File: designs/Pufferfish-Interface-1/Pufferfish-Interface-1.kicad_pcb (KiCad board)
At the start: 2 copper layers, 0 parts

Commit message: beginning layout
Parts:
- added BUZZ1: BUZZER-MALLORY, Pufferfish:Buzzer-MSS5MMG, F.Cu at (95.2, 69.8)
- added BUZZ2: BUZZER, Pufferfish:Buzzer_PS1927P02, F.Cu at (127.0, 68.6)
- added C1: 0.1uF, Pufferfish:CAP_SMD_0805, F.Cu at (121.5, 150.1)
- added C2: 0.1uF, Pufferfish:CAP_SMD_0805, F.Cu at (117.1, 153.0)
- added CONN1: 5103308-3, Pufferfish:SHDR16W66P254_2X8, F.Cu at (186.8, 98.8)
- added CONN2: B2B-PH-SM4-TB(LF)(SN), Pufferfish:JST_B2B-PH-SM4-TB, F.Cu at (109.8, 151.2)
- added CONN3: B2B-PH-SM4-TB(LF)(SN), Pufferfish:JST_B2B-PH-SM4-TB, F.Cu at (99.8, 151.2)
- added D1: 1N4001, Diode_THT:D_DO-41_SOD81_P10.16mm_Horizontal, F.Cu at (96.6, 121.1)
- added D10: LED_RGBA, Pufferfish:LED_D10.0mm-4_RGB, F.Cu at (149.1, 100.7)
- added D2: 1N4001, Diode_THT:D_DO-41_SOD81_P10.16mm_Horizontal, F.Cu at (110.5, 121.1)
- added D3: LED, Pufferfish:LED_SMD_1411_3528, F.Cu at (126.4, 121.2)
- added D4: LED, Pufferfish:LED_SMD_1411_3528, F.Cu at (106.2, 125.4)
- added D5: LED, Pufferfish:LED_SMD_1411_3528, F.Cu at (98.6, 125.4)
- added D6: TPD1E1B04, Pufferfish:D_0402_TPD1E1B04DPYR, F.Cu at (120.7, 152.5)
- added D7: TPD1E1B04, Pufferfish:D_0402_TPD1E1B04DPYR, F.Cu at (125.1, 148.6)
- added D8: TPD1E1B04, Pufferfish:D_0402_TPD1E1B04DPYR, F.Cu at (128.2, 144.4)
- added D9: TPD1E1B04, Pufferfish:D_0402_TPD1E1B04DPYR, F.Cu at (125.1, 146.6)
- added Q1: DMN10H220L, Package_TO_SOT_SMD:SOT-23, F.Cu at (118.7, 125.5)
- added Q10: 2N7002E, Package_TO_SOT_SMD:SOT-23, F.Cu at (132.1, 125.8)
- added Q2: DMN10H220L, Package_TO_SOT_SMD:SOT-23, F.Cu at (145.4, 108.9)
- added Q3: DMN10H220L, Package_TO_SOT_SMD:SOT-23, F.Cu at (132.4, 121.2)
- added Q4: 2SC1815, Package_TO_SOT_THT:TO-92_Inline, F.Cu at (112.0, 126.5)
- added Q5: 2N7002E, Package_TO_SOT_SMD:SOT-23, F.Cu at (123.2, 125.6)
- added Q6: 2N7002E, Package_TO_SOT_SMD:SOT-23, F.Cu at (157.3, 97.0)
- added Q7: 2N7002E, Package_TO_SOT_SMD:SOT-23, F.Cu at (127.6, 125.6)
- added Q8: 2N7002E, Package_TO_SOT_SMD:SOT-23, F.Cu at (145.4, 113.5)
- added Q9: 2N7002E, Package_TO_SOT_SMD:SOT-23, F.Cu at (136.9, 121.2)
- added R1: RES_SMD_0805, Pufferfish:RES_SMD_0805, F.Cu at (157.3, 103.7)
- added R10: RES_SMD_0805, Pufferfish:RES_SMD_0805, F.Cu at (127.5, 129.4)
- added R11: RES_SMD_0805, Pufferfish:RES_SMD_0805, F.Cu at (123.1, 129.4)
- added R12: RES_SMD_0805, Pufferfish:RES_SMD_0805, F.Cu at (118.7, 129.2)
- added R13: RES_SMD_0805, Pufferfish:RES_SMD_0805, F.Cu at (129.0, 136.0)
- added R14: RES_SMD_0805, Pufferfish:RES_SMD_0805, F.Cu at (117.1, 147.1)
- added R15: RES_SMD_0805, Pufferfish:RES_SMD_0805, F.Cu at (129.0, 139.0)
- added R16: RES_SMD_0805, Pufferfish:RES_SMD_0805, F.Cu at (117.1, 150.1)
- added R17: RES_SMD_0805, Pufferfish:RES_SMD_0805, F.Cu at (121.5, 147.1)
- added R18: RES_SMD_0805, Pufferfish:RES_SMD_0805, F.Cu at (129.0, 141.9)
- added R19: RES_SMD_0805, Pufferfish:RES_SMD_0805, F.Cu at (105.8, 129.1)
- added R2: RES_SMD_0805, Pufferfish:RES_SMD_0805, F.Cu at (154.2, 108.1)
- added R20: RES_SMD_0805, Pufferfish:RES_SMD_0805, F.Cu at (157.3, 100.8)
- added R21: RES_SMD_0805, Pufferfish:RES_SMD_0805, F.Cu at (97.0, 129.1)
- added R22: RES_SMD_0805, Pufferfish:RES_SMD_0805, F.Cu at (101.4, 129.1)
- added R23: RES_SMD_0805, Pufferfish:RES_SMD_0805, F.Cu at (149.8, 108.1)
- added R24: RES_SMD_0805, Pufferfish:RES_SMD_0805, F.Cu at (145.4, 117.2)
- added R3: RES_SMD_0805, Pufferfish:RES_SMD_0805, F.Cu at (149.8, 111.1)
- added R4: RES_SMD_0805, Pufferfish:RES_SMD_0805, F.Cu at (136.5, 125.0)
- added R5: RES_SMD_0805, Pufferfish:RES_SMD_0805, F.Cu at (131.9, 129.5)
- added R6: RES_SMD_0805, Pufferfish:RES_SMD_0805, F.Cu at (141.3, 120.4)
- added R7: RES_SMD_0805, Pufferfish:RES_SMD_0805, F.Cu at (141.3, 123.4)
- added R8: RES_SMD_0805, Pufferfish:RES_SMD_0805, F.Cu at (136.5, 127.9)
- added R9: RES_SMD_0805, Pufferfish:RES_SMD_0805, F.Cu at (154.2, 111.1)
- added SW1: SW_Push, Pufferfish:SW_SPST_SMD_5ESH935, F.Cu at (102.8, 140.1)
- added SW2: SW_Push, Pufferfish:SW_SPST_SMD_5ESH935, F.Cu at (118.8, 140.1)

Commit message: placement started
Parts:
- moved R16 171.2 mm to (261.6, 58.4)
- moved SW2 164.9 mm to (266.7, 67.3)
- moved R17 155.8 mm to (268.0, 94.0)
- moved SW1 152.8 mm to (237.4, 67.7)
- moved C2 149.9 mm to (254.3, 92.7)
- moved D9 139.6 mm to (246.4, 77.5), turned to 90 degrees
- moved C1 136.6 mm to (241.0, 83.8)
- moved D7 127.8 mm to (240.0, 92.7)
- moved R13 117.2 mm to (221.0, 63.5)
- moved R15 117.0 mm to (226.1, 73.7)
- moved Q8 106.1 mm to (47.0, 73.7), turned to 90 degrees
- moved R5 92.7 mm to (133.7, 36.8)
- moved D10 92.2 mm to (64.8, 63.5)
- moved Q4 90.4 mm to (193.0, 86.4), turned to 90 degrees
- moved R24 87.2 mm to (69.8, 73.7)
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
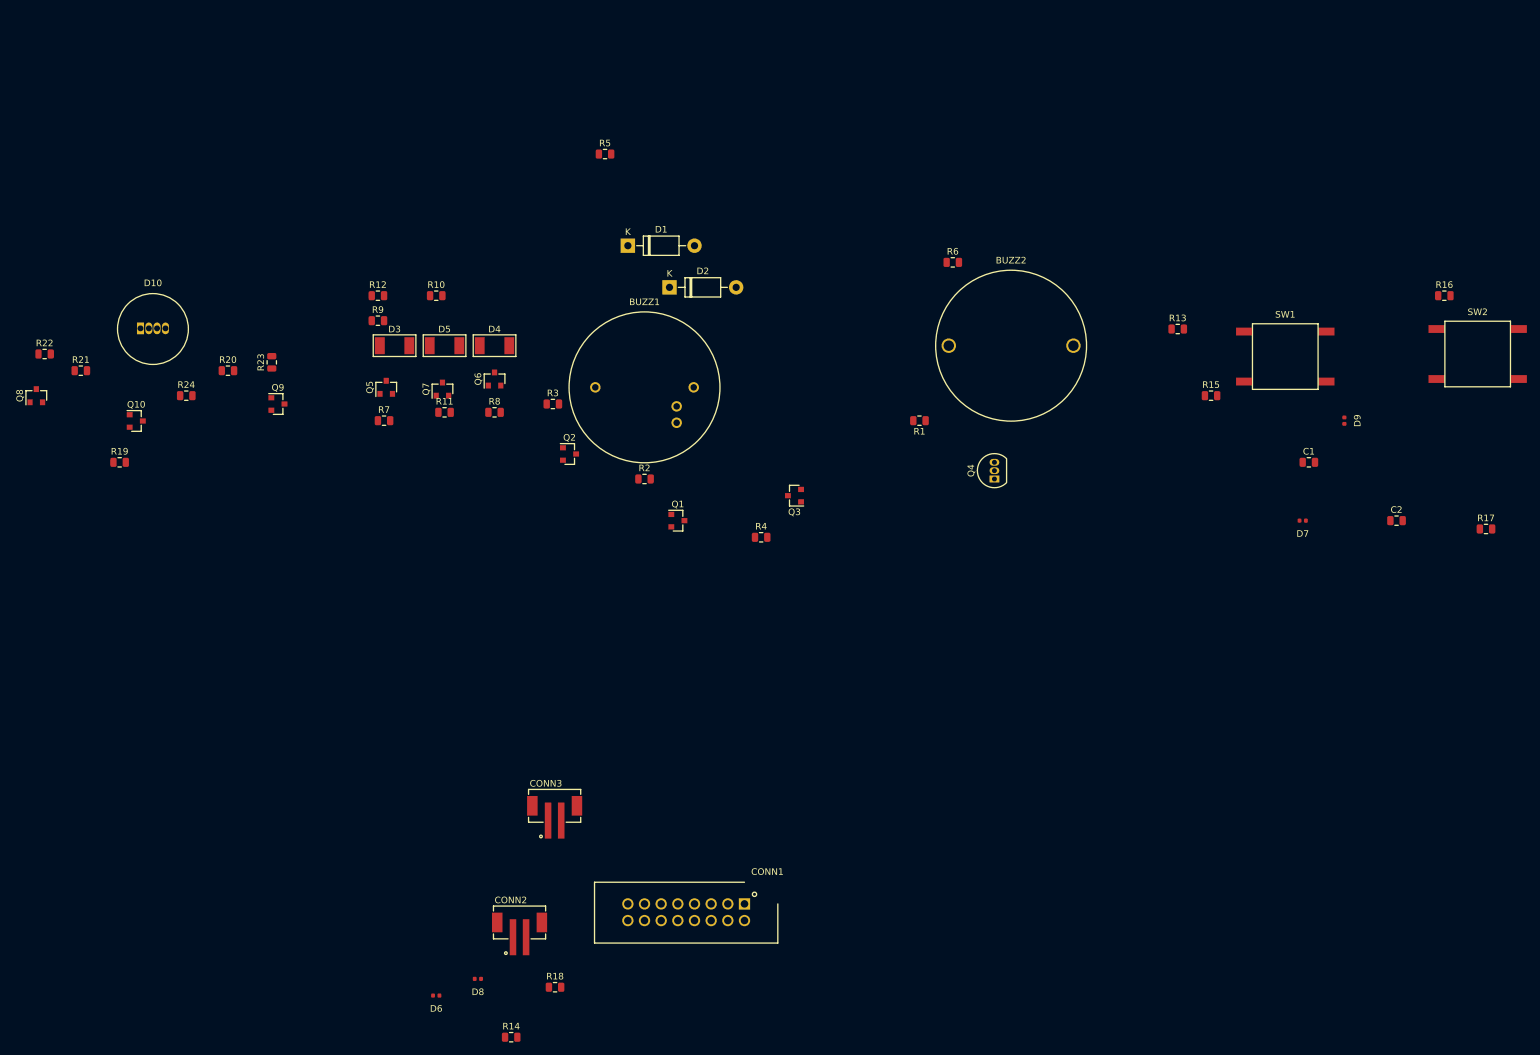
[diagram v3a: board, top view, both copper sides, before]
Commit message: new switches and pcb layout started
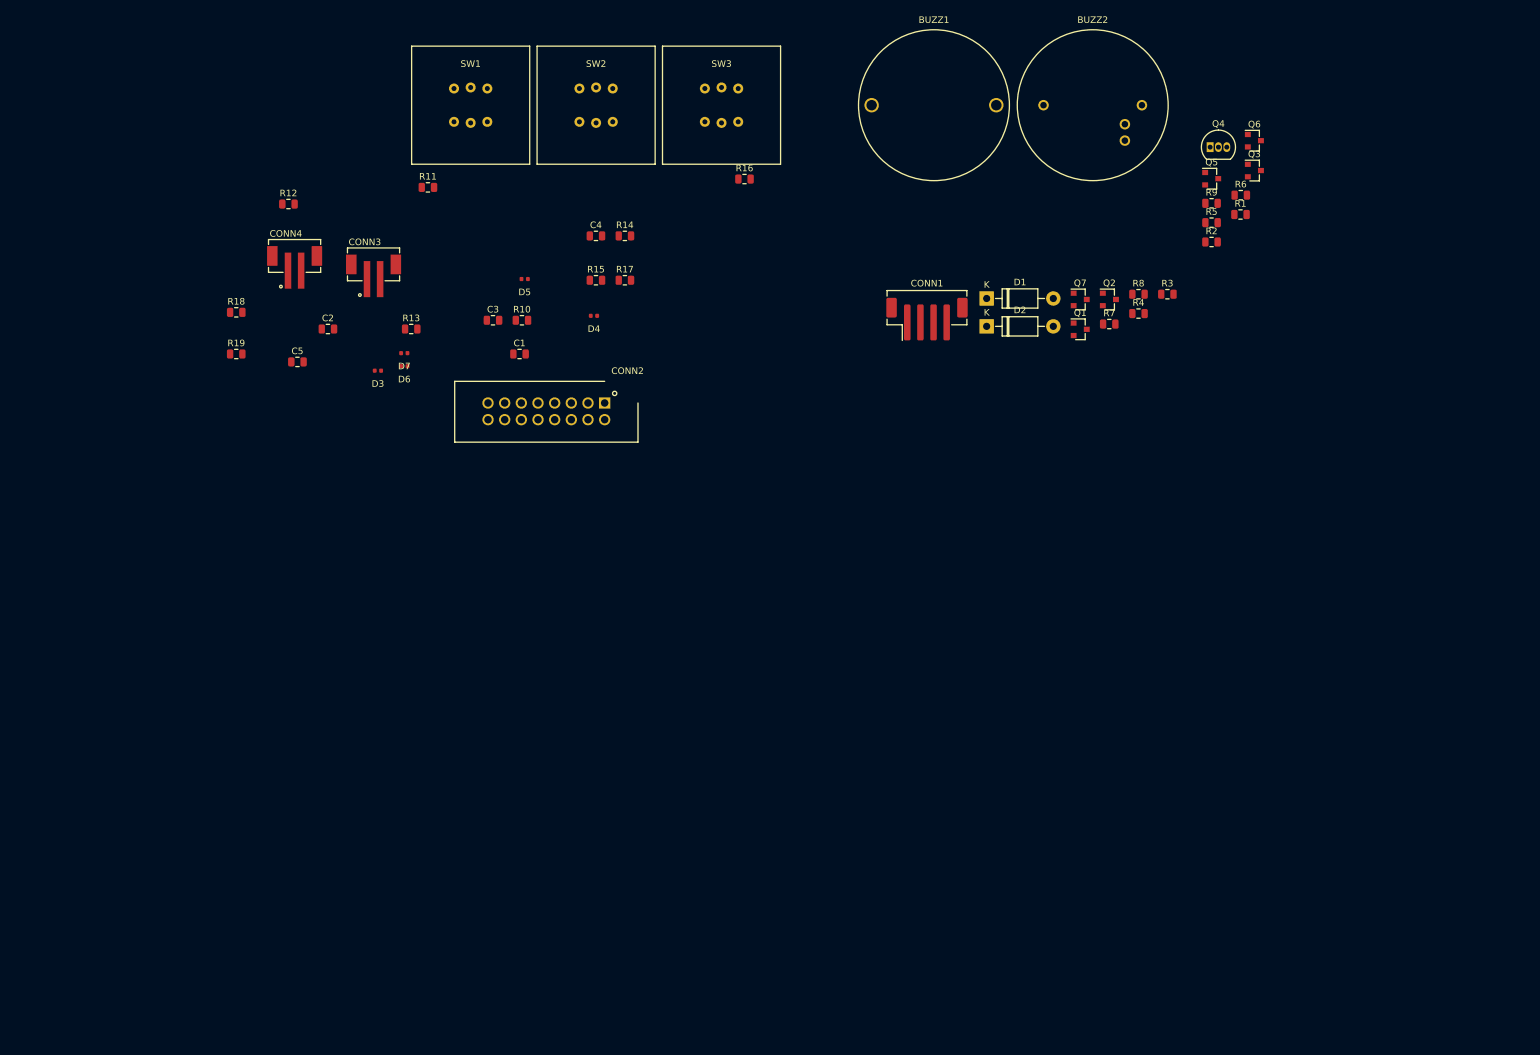
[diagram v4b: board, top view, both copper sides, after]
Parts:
- removed D10: LED_RGBA, Pufferfish:LED_D10.0mm-4_RGB
- removed D8, D9: TPD1E1B04, Pufferfish:D_0402_TPD1E1B04DPYR
- removed Q10, Q8, Q9: 2N7002E, Package_TO_SOT_SMD:SOT-23
- removed R20, R21, R22, R23, R24: RES_SMD_0805, Pufferfish:RES_SMD_0805
- added C3: 0.1uF, Pufferfish:CAP_SMD_0805, F.Cu at (116.6, 62.2)
- added C4: 0.1uF, Pufferfish:CAP_SMD_0805, F.Cu at (132.3, 49.3)
- added C5: 0.1uF, Pufferfish:CAP_SMD_0805, F.Cu at (86.8, 68.5)
- added CONN4: B2B-PH-SM4-TB(LF)(SN), Pufferfish:JST_B2B-PH-SM4-TB, F.Cu at (86.4, 54.6)
- added SW3: SW_Push, Pufferfish:SW_SPST_TC013, F.Cu at (151.4, 29.4)
- BUZZ1: value BUZZER-MALLORY -> BUZZER; footprint Pufferfish:Buzzer-MSS5MMG -> Pufferfish:Buzzer_PS1927P02
- BUZZ2: value BUZZER -> BUZZER-MALLORY; footprint Pufferfish:Buzzer_PS1927P02 -> Pufferfish:Buzzer-MSS5MMG
- CONN1: value 5103308-3 -> B4B-PH-SM4-TB(LF)(SN); footprint Pufferfish:SHDR16W66P254_2X8 -> Connector_JST:JST_PH_B4B-PH-SM4-TB_1x04-1MP_P2.00mm_Vertical
- CONN2: value B2B-PH-SM4-TB(LF)(SN) -> 5103308-3; footprint Pufferfish:JST_B2B-PH-SM4-TB -> Pufferfish:SHDR16W66P254_2X8
- D3, D4, D5: value LED -> TPD1E1B04; footprint Pufferfish:LED_SMD_1411_3528 -> Pufferfish:D_0402_TPD1E1B04DPYR
- SW1, SW2: footprint Pufferfish:SW_SPST_SMD_5ESH935 -> Pufferfish:SW_SPST_TC013
- moved C2 165.5 mm to (91.4, 63.5)
- moved SW2 139.6 mm to (132.3, 29.4)
- moved D7 139.3 mm to (103.1, 67.2)
- moved R17 136.6 mm to (136.7, 56.1)
- moved SW1 129.9 mm to (113.2, 29.4)
- moved Q5 129.8 mm to (226.2, 40.6), turned to 0 degrees
- moved R9 128.3 mm to (226.1, 44.3)
- moved R14 123.4 mm to (136.7, 49.3)
- moved C1 121.4 mm to (120.7, 67.3)
- moved Q6 121.4 mm to (232.7, 34.8), turned to 0 degrees
- moved R13 116.8 mm to (104.1, 63.5)
- moved R18 113.8 mm to (77.5, 61.0)
- moved R7 111.5 mm to (210.5, 62.7)
- moved R16 108.2 mm to (154.9, 40.6)
- moved R8 99.8 mm to (215.0, 58.2)
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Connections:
- BUZZ1 pad 1: 5V -> Net-(BUZZ1-Pad1)
- C2 pad 1: SET_NOT_PAUSE -> SET_PWR_ON_OFF
- CONN1 pad 2: 5V -> Net-(CONN1-Pad2)
- CONN1 pad 3: GND -> Net-(CONN1-Pad3)
- CONN1 pad 4: 3.3V -> Net-(CONN1-Pad4)
- CONN1 pad 5: ALARM2_CNTRL -> Net-(CONN1-Pad5)
- CONN1 pad 6: GND -> Net-(CONN1-Pad5)
- CONN2 pad 1: SET_PWR_ON_OFF -> 5V
- CONN2 pad 2: 3.3V -> 5V
- CONN2 pad 3: Net-(CONN2-Pad3) -> GND
- CONN2 pad 4: Net-(CONN2-Pad3) -> 3.3V
- CONN3 pad 1: SET_PWR_SRC -> GND
- CONN3 pad 2: 3.3V -> Net-(CONN3-Pad2)
- D1 pad 1: Net-(BUZZ1-Pad2) -> Net-(BUZZ2-Pad2)
- D1 pad 2: Net-(BUZZ1-Pad4) -> Net-(BUZZ2-Pad4)
- D2 pad 1: Net-(BUZZ1-Pad3) -> Net-(BUZZ2-Pad3)
- D2 pad 2: Net-(BUZZ1-Pad4) -> Net-(BUZZ2-Pad4)
- D3 pad 1: Net-(D3-Pad1) -> SET_ALARM_EN
- D3 pad 2: Net-(D3-Pad2) -> GND
- D4 pad 1: Net-(D4-Pad1) -> SET_PWR_ON_OFF
- D4 pad 2: Net-(D4-Pad2) -> GND
- D5 pad 1: Net-(D5-Pad1) -> SET_NOT_PAUSE
- D5 pad 2: Net-(D5-Pad2) -> GND
- D6 pad 1: SET_PWR_ON_OFF -> SET_EXTRA1
- D7 pad 1: SET_ALARM_EN -> SET_PWR_SRC
- Q1 pad 3: Net-(BUZZ1-Pad2) -> Net-(BUZZ2-Pad2)
- Q2 pad 3: Net-(BUZZ1-Pad3) -> Net-(BUZZ2-Pad3)
- Q3 pad 3: Net-(BUZZ1-Pad4) -> Net-(BUZZ2-Pad4)
- Q4 pad 2: Net-(BUZZ2-Pad-) -> Net-(BUZZ1-Pad2)
- Q5 pad 1: LEDR_EN -> LEDG_EN
- Q5 pad 3: Net-(D3-Pad1) -> Net-(CONN1-Pad2)
- Q6 pad 1: LEDG_EN -> LEDR_EN
- Q6 pad 3: Net-(D4-Pad1) -> Net-(CONN1-Pad3)
- Q7 pad 1: LEDY_EN -> LEDB_EN
- Q7 pad 3: Net-(D5-Pad1) -> Net-(CONN1-Pad4)
- R1 pad 1: Net-(Q4-Pad3) -> ALARM1_HIGH
- R1 pad 2: ALARM2_CNTRL -> Net-(R1-Pad2)
- R10 pad 2: Net-(D4-Pad2) -> Net-(R10-Pad2)
- R11 pad 1: LEDY_EN -> Net-(R10-Pad2)
- R11 pad 2: Net-(R11-Pad2) -> SET_ALARM_EN
- R12 pad 2: Net-(D5-Pad2) -> Net-(CONN3-Pad2)
- R13 pad 1: 3.3V -> Net-(CONN3-Pad2)
- R13 pad 2: Net-(R13-Pad2) -> SET_PWR_ON_OFF
- R14 pad 1: SET_PWR_ON_OFF -> 3.3V
- R14 pad 2: GND -> Net-(R14-Pad2)
- R15 pad 1: Net-(R13-Pad2) -> Net-(R14-Pad2)
- R15 pad 2: SET_ALARM_EN -> SET_NOT_PAUSE
- R17 pad 2: SET_NOT_PAUSE -> SET_EXTRA1
- R18 pad 1: SET_PWR_SRC -> 3.3V
- R18 pad 2: GND -> Net-(CONN4-Pad2)
- R19 pad 1: LEDR_EN -> Net-(CONN4-Pad2)
- R19 pad 2: Net-(R19-Pad2) -> SET_PWR_SRC
- R2 pad 1: ALARM1_HIGH -> ALARM1_MED
- R3 pad 1: ALARM1_MED -> ALARM1_LOW
- R4 pad 1: ALARM1_LOW -> Net-(Q4-Pad3)
- R4 pad 2: Net-(R4-Pad2) -> ALARM2_CNTRL
- R5 pad 2: Net-(BUZZ2-Pad+) -> Net-(BUZZ1-Pad1)
- R6 pad 1: Net-(BUZZ2-Pad+) -> Net-(BUZZ1-Pad1)
- R6 pad 2: Net-(BUZZ2-Pad-) -> Net-(BUZZ1-Pad2)
- R7 pad 1: LEDR_EN -> LEDG_EN
- R8 pad 1: LEDG_EN -> LEDR_EN
- R9 pad 1: 3.3V -> LEDB_EN
- R9 pad 2: Net-(D3-Pad2) -> Net-(R9-Pad2)
- SW1 pad 2: Net-(R13-Pad2) -> Net-(R10-Pad2)
- SW2 pad 2: Net-(R16-Pad2) -> Net-(R14-Pad2)

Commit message: board layout in progress
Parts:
- removed the C3 at (116.6, 62.2)
- removed CONN4: B2B-PH-SM4-TB(LF)(SN), Pufferfish:JST_B2B-PH-SM4-TB
- removed the D5 at (121.4, 55.9)
- removed the R14 at (136.7, 49.3)
- removed the R16 at (154.9, 40.6)
- removed the R17 at (136.7, 56.1)
- added C2: 0.1uF, Pufferfish:CAP_SMD_0805, B.Cu at (15.2, 3.81)
- added D4: TPD1E1B04, Pufferfish:D_0402_TPD1E1B04DPYR, B.Cu at (15.2, 19.1)
- added R10: RES_SMD_0805, Pufferfish:RES_SMD_0805, B.Cu at (36.8, 19.1)
- added R11: RES_SMD_0805, Pufferfish:RES_SMD_0805, B.Cu at (17.8, 21.6)
- added R13: RES_SMD_0805, Pufferfish:RES_SMD_0805, B.Cu at (26.3, 24.1)
- added R20: RES_SMD_0805, Pufferfish:RES_SMD_0805, B.Cu at (12.7, 24.1)
- added R21: RES_SMD_0805, Pufferfish:RES_SMD_0805, B.Cu at (50.8, 21.6)
- added R22: RES_SMD_0805, Pufferfish:RES_SMD_0805, B.Cu at (5.08, 26.7)
- added R23: RES_SMD_0805, Pufferfish:RES_SMD_0805, B.Cu at (45.4, 20.3)
- added SW4: SW_SPST_LED, Pufferfish:SW_SPST_TC013, F.Cu at (53.3, 11.4)
- C1, C4, C5, CONN2, CONN3, D3, D6, D7, Q4, Q5, Q6, Q7, R15, R18, R19, R4, R7, R8, R9: moved to B.Cu
- C3: renamed from C2; moved to B.Cu
- CONN1: footprint Connector_JST:JST_PH_B4B-PH-SM4-TB_1x04-1MP_P2.00mm_Vertical -> Pufferfish:JST_B4B-PH-SM4-TB; moved to B.Cu
- D5: renamed from D4; moved to B.Cu
- R12: renamed from R10; moved to B.Cu
- R14: renamed from R11; moved to B.Cu
- R16: renamed from R12; moved to B.Cu
- R17: renamed from R13; moved to B.Cu
- SW1, SW2, SW3: value SW_Push -> SW_SPST_LED
- moved Q6 182.6 mm to (57.1, 85.1), turned to 270 degrees
- moved R9 181.4 mm to (48.3, 80.0), turned to 180 degrees
- moved Q5 169.5 mm to (61.0, 78.7), turned to 270 degrees
- moved R7 168.3 mm to (43.2, 80.0), turned to 180 degrees
- moved Q4 167.3 mm to (62.2, 1.27), turned to 270 degrees
- moved R8 162.8 mm to (53.7, 80.0), turned to 180 degrees
- moved Q7 159.0 mm to (49.5, 86.4), turned to 270 degrees
- moved R4 156.6 mm to (63.5, 21.6)
- moved R2 148.9 mm to (78.7, 29.2)
- moved R5 146.4 mm to (86.4, 3.81), turned to 180 degrees
- moved SW3 146.2 mm to (6.35, 11.4)
- moved R6 145.8 mm to (86.4, 21.6), turned to 180 degrees
- moved C4 142.0 mm to (-2.21, 3.81), turned to 90 degrees
- moved R1 136.3 mm to (95.6, 26.7)
- moved D5 135.1 mm to (-2.54, 73.7)
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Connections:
- net SET_NOT_PAUSE renamed SET_LOCK
- C5 pad 1: SET_PWR_SRC -> SET_EXTRA2
- CONN2 pad 15: SET_PWR_ON_OFF -> SET_EXTRA1
- CONN2 pad 6: SET_EXTRA1 -> SET_EXTRA2
- D7 pad 1: SET_PWR_SRC -> SET_EXTRA2
- R12 pad 2: Net-(R10-Pad2) -> Net-(R12-Pad2)
- R14 pad 1: Net-(R10-Pad2) -> Net-(R12-Pad2)
- R15 pad 1: Net-(R14-Pad2) -> Net-(R13-Pad2)
- R18 pad 2: Net-(CONN4-Pad2) -> Net-(R18-Pad2)
- R19 pad 1: Net-(CONN4-Pad2) -> 3.3V
- R19 pad 2: SET_PWR_SRC -> Net-(R19-Pad2)
- SW1 pad 1: GND -> Net-(R12-Pad2)
- SW1 pad 2: Net-(R10-Pad2) -> GND
- SW1 pad 3: (no net) -> Net-(R12-Pad2)
- SW2 pad 1: GND -> Net-(R13-Pad2)
- SW2 pad 2: Net-(R14-Pad2) -> GND
- SW2 pad 3: (no net) -> Net-(R13-Pad2)
- SW3 pad 1: GND -> Net-(R20-Pad2)
- SW3 pad 2: Net-(R16-Pad2) -> GND
- SW3 pad 3: (no net) -> Net-(R20-Pad2)
